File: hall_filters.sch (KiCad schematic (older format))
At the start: 11 parts

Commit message: - updated project to 5.0.0 - added ignore file
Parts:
- C13, C14, C15, C16: symbol C-RESCUE-BLDC_4 -> HSWR-V2-rescue:C-RESCUE-BLDC_4
- R32, R33, R34, R35, R36, R37, R38: symbol R-RESCUE-BLDC_4 -> HSWR-V2-rescue:R-RESCUE-BLDC_4
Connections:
- wire segments 20 -> 31
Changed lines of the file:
@@
-EESchema Schematic File Version 2
-LIBS:HSWR V2-rescue
-LIBS:power
-LIBS:device
-LIBS:transistors
-LIBS:conn
-LIBS:linear
-LIBS:regul
-LIBS:74xx
-LIBS:cmos4000
-LIBS:adc-dac
-LIBS:memory
-LIBS:xilinx
-LIBS:microcontrollers
-LIBS:dsp
-LIBS:microchip
-LIBS:analog_switches
-LIBS:motorola
-LIBS:texas
-LIBS:intel
-LIBS:audio
-LIBS:interface
-LIBS:digital-audio
-LIBS:philips
-LIBS:display
-LIBS:cypress
-LIBS:siliconi
-LIBS:opto
-LIBS:atmel
-LIBS:contrib
-LIBS:valves
+EESchema Schematic File Version 4
 LIBS:HSWR V2-cache
-EELAYER 25 0
+EELAYER 26 0
 EELAYER END
 $Descr A4 11693 8268
@@
 $EndDescr
 $Comp
-L R-RESCUE-BLDC_4 R32
+L HSWR-V2-rescue:R-RESCUE-BLDC_4 R32
 U 1 1 53FBB581
 P 4900 3200
@@
 $EndComp
 $Comp
-L R-RESCUE-BLDC_4 R38
+L HSWR-V2-rescue:R-RESCUE-BLDC_4 R38
 U 1 1 53FBB588
 P 5550 3750
@@
 $EndComp
 $Comp
-L R-RESCUE-BLDC_4 R37
+L HSWR-V2-rescue:R-RESCUE-BLDC_4 R37
 U 1 1 53FBB58F
 P 5550 3650
@@
 $EndComp
 $Comp
-L R-RESCUE-BLDC_4 R36
+L HSWR-V2-rescue:R-RESCUE-BLDC_4 R36
 U 1 1 53FBB596
 P 5550 3550
@@
 $EndComp
 $Comp
-L C-RESCUE-BLDC_4 C14
+L HSWR-V2-rescue:C-RESCUE-BLDC_4 C14
 U 1 1 53FBB59D
 P 5950 4250
@@
 $EndComp
 $Comp
-L C-RESCUE-BLDC_4 C15
+L HSWR-V2-rescue:C-RESCUE-BLDC_4 C15
 U 1 1 53FBB5A4
 P 6200 4250
@@
 $EndComp
 $Comp
-L C-RESCUE-BLDC_4 C16
+L HSWR-V2-rescue:C-RESCUE-BLDC_4 C16
 U 1 1 53FBB5AB
 P 6450 4250
@@
 $EndComp
 $Comp
-L GND-RESCUE-BLDC_4 #PWR034
+L HSWR-V2-rescue:GND-RESCUE-BLDC_4 #PWR034
 U 1 1 53FBB5B2
 P 5950 4450
@@
 $EndComp
 $Comp
-L R-RESCUE-BLDC_4 R33
+L HSWR-V2-rescue:R-RESCUE-BLDC_4 R33
 U 1 1 53FBB5B8
 P 5000 3200
@@
 $EndComp
 $Comp
-L R-RESCUE-BLDC_4 R34
+L HSWR-V2-rescue:R-RESCUE-BLDC_4 R34
 U 1 1 53FBB5BF
 P 5100 3200
@@
 $EndComp
 $Comp
-L R-RESCUE-BLDC_4 R35
+L HSWR-V2-rescue:R-RESCUE-BLDC_4 R35
 U 1 1 53FBB5C6
 P 5200 3200
@@
 $EndComp
 $Comp
-L C-RESCUE-BLDC_4 C13
+L HSWR-V2-rescue:C-RESCUE-BLDC_4 C13
 U 1 1 53FBB5CD
 P 5100 4250
@@
 $EndComp
 $Comp
-L GND-RESCUE-BLDC_4 #PWR035
+L HSWR-V2-rescue:GND-RESCUE-BLDC_4 #PWR035
 U 1 1 53FBB5D4
 P 5100 4450
@@
 	5200 3450 5200 3750
 Wire Wire Line
-	4800 3750 5300 3750
-Wire Wire Line
-	4800 3650 5300 3650
-Wire Wire Line
-	4800 3550 5300 3550
+	4800 3750 5200 3750
+Wire Wire Line
+	4800 3650 5100 3650
+Wire Wire Line
+	4800 3550 5000 3550
 Wire Wire Line
 	6450 3750 6450 4050
 Wire Wire Line
-	5800 3750 6600 3750
+	5800 3750 6450 3750
 Wire Wire Line
 	6200 3650 6200 4050
 Wire Wire Line
-	5800 3650 6600 3650
+	5800 3650 6200 3650
 Wire Wire Line
 	5950 3550 5950 4050
 Wire Wire Line
-	5800 3550 6600 3550
+	5800 3550 5950 3550
 Wire Wire Line
 	5100 3850 5100 4050
 $Comp
-L GND-RESCUE-BLDC_4 #PWR036
+L HSWR-V2-rescue:GND-RESCUE-BLDC_4 #PWR036
 U 1 1 53FBB5F9
 P 6200 4450
@@
 $EndComp
 $Comp
-L GND-RESCUE-BLDC_4 #PWR037
+L HSWR-V2-rescue:GND-RESCUE-BLDC_4 #PWR037
 U 1 1 53FBB5FF
 P 6450 4450
@@
 Connection ~ 4900 3850
 Wire Wire Line
-	4900 2750 4900 2950
-Wire Wire Line
-	4900 2850 5200 2850
+	4900 2750 4900 2850
+Wire Wire Line
+	4900 2850 5000 2850
 Connection ~ 5000 2850
 Connection ~ 5100 2850
 Wire Wire Line
-	4800 3850 6600 3850
+	4800 3850 4900 3850
 Connection ~ 5100 3850
 Text HLabel 4800 3550 0    60   Input ~ 0
@@
 TEMP_OUT
 $Comp
-L +3V3 #PWR038
+L power:+3V3 #PWR038
 U 1 1 5752258C
 P 4900 2750
@@
 $EndComp
 Connection ~ 4900 2850
+Wire Wire Line
+	5950 3550 6600 3550
+Wire Wire Line
+	6200 3650 6600 3650
+Wire Wire Line
+	6450 3750 6600 3750
+Wire Wire Line
+	5000 3550 5300 3550
+Wire Wire Line
+	5100 3650 5300 3650
+Wire Wire Line
+	5200 3750 5300 3750
+Wire Wire Line
+	4900 3850 5100 3850
+Wire Wire Line
+	5000 2850 5100 2850
+Wire Wire Line
+	5100 2850 5200 2850
+Wire Wire Line
+	5100 3850 6600 3850
+Wire Wire Line
+	4900 2850 4900 2950
 $EndSCHEMATC

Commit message: - updated to VESC6 architecture - still some things to do in schematic
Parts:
- removed C13, C14, C15, C16: 4n7, Capacitors_SMD:C_0805, symbol HSWR-V2-rescue:C-RESCUE-BLDC_4
- removed R32, R36, R37, R38: 10k, Resistors_SMD:R_0805, symbol HSWR-V2-rescue:R-RESCUE-BLDC_4
- removed R33, R34, R35: 2k2, Resistors_SMD:R_0805, symbol HSWR-V2-rescue:R-RESCUE-BLDC_4
- added C1, C3, C4, C5: 4n7, Capacitor_SMD:C_0805_2012Metric, symbol Device:C
- added R12, R18, R19, R20: 10k, Resistor_SMD:R_0805_2012Metric, symbol Device:R
- added R13, R14, R15: 2k2, Resistor_SMD:R_0805_2012Metric, symbol Device:R
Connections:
- wire segments 31 -> 30

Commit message: - rescued schematic - added *.sch-bak to ignore - fixed bypass diode polarity - fixed PDEN being low - added 0R resistors instead of USB iso option - added caps to DCDC - added filter to VDDA
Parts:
- C1, C3, C4, C5: symbol Device:C -> HSWR-V2-rescue:C-Device
- R12, R13, R14, R15, R18, R19, R20: symbol Device:R -> HSWR-V2-rescue:R-Device
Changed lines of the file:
@@
 EESchema Schematic File Version 4
-LIBS:HSWR V2-cache
-EELAYER 26 0
+EELAYER 30 0
 EELAYER END
 $Descr A4 11693 8268
@@
 TEMP_OUT
 $Comp
-L power:+3V3 #PWR038
+L HSWR-V2-rescue:+3V3-power #PWR038
 U 1 1 5752258C
 P 4900 2950
@@
 	4900 3050 4900 3150
 $Comp
-L Device:R R?
+L HSWR-V2-rescue:R-Device R?
 U 1 1 5C9EFE99
 P 4900 3300
@@
 $EndComp
 $Comp
-L Device:R R?
+L HSWR-V2-rescue:R-Device R?
 U 1 1 5C9F02C4
 P 5100 3300
@@
 	4800 4050 4900 4050
 $Comp
-L Device:R R?
+L HSWR-V2-rescue:R-Device R?
 U 1 1 5C9F1880
 P 5300 3300
@@
 $EndComp
 $Comp
-L Device:R R?
+L HSWR-V2-rescue:R-Device R?
 U 1 1 5C9F189A
 P 5500 3300
@@
 $EndComp
 $Comp
-L Device:R R?
+L HSWR-V2-rescue:R-Device R?
 U 1 1 5C9F21C4
 P 5750 3550
@@
 $EndComp
 $Comp
-L Device:R R?
+L HSWR-V2-rescue:R-Device R?
 U 1 1 5C9F262F
 P 5750 3750
@@
 $EndComp
 $Comp
-L Device:R R?
+L HSWR-V2-rescue:R-Device R?
 U 1 1 5C9F2B46
 P 5750 3950
@@
 	4900 4050 6700 4050
 $Comp
-L Device:C C3
+L HSWR-V2-rescue:C-Device C3
 U 1 1 5C9F2C75
 P 6050 4300
@@
 $EndComp
 $Comp
-L power:GND #PWR0117
+L HSWR-V2-rescue:GND-power #PWR0117
 U 1 1 5C9F2CD2
 P 6050 4450
@@
 	4900 4050 4900 4150
 $Comp
-L Device:C C1
+L HSWR-V2-rescue:C-Device C1
 U 1 1 5C9F3D39
 P 4900 4300
@@
 $EndComp
 $Comp
-L power:GND #PWR0118
+L HSWR-V2-rescue:GND-power #PWR0118
 U 1 1 5C9F3D40
 P 4900 4450
@@
 $EndComp
 $Comp
-L power:GND #PWR0119
+L HSWR-V2-rescue:GND-power #PWR0119
 U 1 1 5C9F4131
 P 6300 4450
@@
 $EndComp
 $Comp
-L Device:C C4
+L HSWR-V2-rescue:C-Device C4
 U 1 1 5C9F467A
 P 6300 4300
@@
 $EndComp
 $Comp
-L Device:C C5
+L HSWR-V2-rescue:C-Device C5
 U 1 1 5C9F46A6
 P 6550 4300
@@
 $EndComp
 $Comp
-L power:GND #PWR0120
+L HSWR-V2-rescue:GND-power #PWR0120
 U 1 1 5C9F46D2
 P 6550 4450

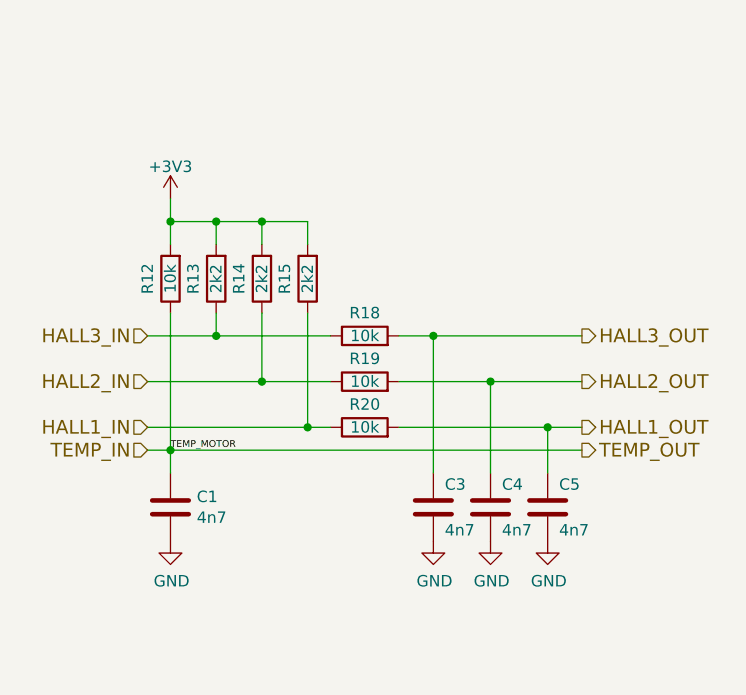
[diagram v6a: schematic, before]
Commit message: - changed CSA for Hall effect sensors - updated power stage layout
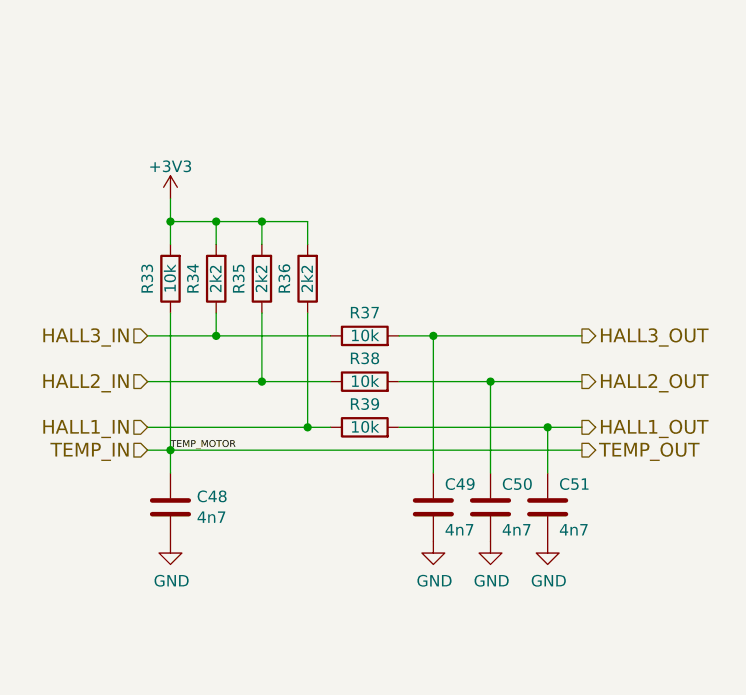
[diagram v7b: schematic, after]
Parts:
- renumbered C1 to C48, C3 to C49, C4 to C50, C5 to C51, R12 to R33, R13 to R34, R14 to R35, R15 to R36, R18 to R37, R19 to R38, R20 to R39
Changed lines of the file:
@@
 TEMP_OUT
 $Comp
-L HSWR-V2-rescue:+3V3-power #PWR038
+L HSWR-V2-rescue:+3V3-power #PWR095
 U 1 1 5752258C
 P 4900 2950
-F 0 "#PWR038" H 4900 2800 50  0001 C CNN
+F 0 "#PWR095" H 4900 2800 50  0001 C CNN
 F 1 "+3V3" H 4900 3090 50  0000 C CNN
 F 2 "" H 4900 2950 60  0000 C CNN
@@
 P 4900 3300
 AR Path="/5895E6A0/5C9EFE99" Ref="R?"  Part="1"
-AR Path="/5899E226/5C9EFE99" Ref="R12"  Part="1"
-F 0 "R12" V 5000 3300 50  0000 C CNN
+AR Path="/5899E226/5C9EFE99" Ref="R33"  Part="1"
+F 0 "R33" V 5000 3300 50  0000 C CNN
 F 1 "10k" V 4900 3300 50  0000 C CNN
 F 2 "Resistor_SMD:R_0805_2012Metric" V 4830 3300 50  0001 C CNN
@@
 P 5100 3300
 AR Path="/5895E6A0/5C9F02C4" Ref="R?"  Part="1"
-AR Path="/5899E226/5C9F02C4" Ref="R13"  Part="1"
-F 0 "R13" V 5200 3300 50  0000 C CNN
+AR Path="/5899E226/5C9F02C4" Ref="R34"  Part="1"
+F 0 "R34" V 5200 3300 50  0000 C CNN
 F 1 "2k2" V 5100 3300 50  0000 C CNN
 F 2 "Resistor_SMD:R_0805_2012Metric" V 5030 3300 50  0001 C CNN
@@
 P 5300 3300
 AR Path="/5895E6A0/5C9F1880" Ref="R?"  Part="1"
-AR Path="/5899E226/5C9F1880" Ref="R14"  Part="1"
-F 0 "R14" V 5400 3300 50  0000 C CNN
+AR Path="/5899E226/5C9F1880" Ref="R35"  Part="1"
+F 0 "R35" V 5400 3300 50  0000 C CNN
 F 1 "2k2" V 5300 3300 50  0000 C CNN
 F 2 "Resistor_SMD:R_0805_2012Metric" V 5230 3300 50  0001 C CNN
@@
 P 5500 3300
 AR Path="/5895E6A0/5C9F189A" Ref="R?"  Part="1"
-AR Path="/5899E226/5C9F189A" Ref="R15"  Part="1"
-F 0 "R15" V 5600 3300 50  0000 C CNN
+AR Path="/5899E226/5C9F189A" Ref="R36"  Part="1"
+F 0 "R36" V 5600 3300 50  0000 C CNN
 F 1 "2k2" V 5500 3300 50  0000 C CNN
 F 2 "Resistor_SMD:R_0805_2012Metric" V 5430 3300 50  0001 C CNN
@@
 P 5750 3550
 AR Path="/5895E6A0/5C9F21C4" Ref="R?"  Part="1"
-AR Path="/5899E226/5C9F21C4" Ref="R18"  Part="1"
-F 0 "R18" V 5850 3550 50  0000 C CNN
+AR Path="/5899E226/5C9F21C4" Ref="R37"  Part="1"
+F 0 "R37" V 5850 3550 50  0000 C CNN
 F 1 "10k" V 5750 3550 50  0000 C CNN
 F 2 "Resistor_SMD:R_0805_2012Metric" V 5680 3550 50  0001 C CNN
@@
 P 5750 3750
 AR Path="/5895E6A0/5C9F262F" Ref="R?"  Part="1"
-AR Path="/5899E226/5C9F262F" Ref="R19"  Part="1"
-F 0 "R19" V 5850 3750 50  0000 C CNN
+AR Path="/5899E226/5C9F262F" Ref="R38"  Part="1"
+F 0 "R38" V 5850 3750 50  0000 C CNN
 F 1 "10k" V 5750 3750 50  0000 C CNN
 F 2 "Resistor_SMD:R_0805_2012Metric" V 5680 3750 50  0001 C CNN
@@
 P 5750 3950
 AR Path="/5895E6A0/5C9F2B46" Ref="R?"  Part="1"
-AR Path="/5899E226/5C9F2B46" Ref="R20"  Part="1"
-F 0 "R20" V 5850 3950 50  0000 C CNN
+AR Path="/5899E226/5C9F2B46" Ref="R39"  Part="1"
+F 0 "R39" V 5850 3950 50  0000 C CNN
 F 1 "10k" V 5750 3950 50  0000 C CNN
 F 2 "Resistor_SMD:R_0805_2012Metric" V 5680 3950 50  0001 C CNN
@@
 	4900 4050 6700 4050
 $Comp
-L HSWR-V2-rescue:C-Device C3
+L HSWR-V2-rescue:C-Device C49
 U 1 1 5C9F2C75
 P 6050 4300
-F 0 "C3" H 6100 4400 50  0000 L CNN
+F 0 "C49" H 6100 4400 50  0000 L CNN
 F 1 "4n7" H 6100 4200 50  0000 L CNN
 F 2 "Capacitor_SMD:C_0805_2012Metric" H 6088 4150 50  0001 C CNN
@@
 $EndComp
 $Comp
-L HSWR-V2-rescue:GND-power #PWR0117
+L HSWR-V2-rescue:GND-power #PWR097
 U 1 1 5C9F2CD2
 P 6050 4450
-F 0 "#PWR0117" H 6050 4200 50  0001 C CNN
+F 0 "#PWR097" H 6050 4200 50  0001 C CNN
 F 1 "GND" H 6055 4277 50  0000 C CNN
 F 2 "" H 6050 4450 50  0001 C CNN
@@
 	4900 4050 4900 4150
 $Comp
-L HSWR-V2-rescue:C-Device C1
+L HSWR-V2-rescue:C-Device C48
 U 1 1 5C9F3D39
 P 4900 4300
-F 0 "C1" H 5015 4346 50  0000 L CNN
+F 0 "C48" H 5015 4346 50  0000 L CNN
 F 1 "4n7" H 5015 4255 50  0000 L CNN
 F 2 "Capacitor_SMD:C_0805_2012Metric" H 4938 4150 50  0001 C CNN
@@
 $EndComp
 $Comp
-L HSWR-V2-rescue:GND-power #PWR0118
+L HSWR-V2-rescue:GND-power #PWR096
 U 1 1 5C9F3D40
 P 4900 4450
-F 0 "#PWR0118" H 4900 4200 50  0001 C CNN
+F 0 "#PWR096" H 4900 4200 50  0001 C CNN
 F 1 "GND" H 4905 4277 50  0000 C CNN
 F 2 "" H 4900 4450 50  0001 C CNN
@@
 $EndComp
 $Comp
-L HSWR-V2-rescue:GND-power #PWR0119
+L HSWR-V2-rescue:GND-power #PWR098
 U 1 1 5C9F4131
 P 6300 4450
-F 0 "#PWR0119" H 6300 4200 50  0001 C CNN
+F 0 "#PWR098" H 6300 4200 50  0001 C CNN
 F 1 "GND" H 6305 4277 50  0000 C CNN
 F 2 "" H 6300 4450 50  0001 C CNN
@@
 $EndComp
 $Comp
-L HSWR-V2-rescue:C-Device C4
+L HSWR-V2-rescue:C-Device C50
 U 1 1 5C9F467A
 P 6300 4300
-F 0 "C4" H 6350 4400 50  0000 L CNN
+F 0 "C50" H 6350 4400 50  0000 L CNN
 F 1 "4n7" H 6350 4200 50  0000 L CNN
 F 2 "Capacitor_SMD:C_0805_2012Metric" H 6338 4150 50  0001 C CNN
@@
 $EndComp
 $Comp
-L HSWR-V2-rescue:C-Device C5
+L HSWR-V2-rescue:C-Device C51
 U 1 1 5C9F46A6
 P 6550 4300
-F 0 "C5" H 6600 4400 50  0000 L CNN
+F 0 "C51" H 6600 4400 50  0000 L CNN
 F 1 "4n7" H 6600 4200 50  0000 L CNN
 F 2 "Capacitor_SMD:C_0805_2012Metric" H 6588 4150 50  0001 C CNN
@@
 $EndComp
 $Comp
-L HSWR-V2-rescue:GND-power #PWR0120
+L HSWR-V2-rescue:GND-power #PWR099
 U 1 1 5C9F46D2
 P 6550 4450
-F 0 "#PWR0120" H 6550 4200 50  0001 C CNN
+F 0 "#PWR099" H 6550 4200 50  0001 C CNN
 F 1 "GND" H 6555 4277 50  0000 C CNN
 F 2 "" H 6550 4450 50  0001 C CNN

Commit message: - removed rescue lib and symbols - added HSWR.lib
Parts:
- C48, C49, C50, C51: symbol HSWR-V2-rescue:C-Device -> Device:C
- R33, R34, R35, R36, R37, R38, R39: symbol HSWR-V2-rescue:R-Device -> Device:R
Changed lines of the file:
@@
 $Descr A4 11693 8268
 encoding utf-8
-Sheet 6 8
+Sheet 5 8
 Title "HSWR HAL Filters"
 Date "2017-02-05"
@@
 TEMP_OUT
 $Comp
-L HSWR-V2-rescue:+3V3-power #PWR095
+L power:+3V3 #PWR095
 U 1 1 5752258C
 P 4900 2950
@@
 	4900 3050 4900 3150
 $Comp
-L HSWR-V2-rescue:R-Device R?
+L Device:R R?
 U 1 1 5C9EFE99
 P 4900 3300
@@
 $EndComp
 $Comp
-L HSWR-V2-rescue:R-Device R?
+L Device:R R?
 U 1 1 5C9F02C4
 P 5100 3300
@@
 	4800 4050 4900 4050
 $Comp
-L HSWR-V2-rescue:R-Device R?
+L Device:R R?
 U 1 1 5C9F1880
 P 5300 3300
@@
 $EndComp
 $Comp
-L HSWR-V2-rescue:R-Device R?
+L Device:R R?
 U 1 1 5C9F189A
 P 5500 3300
@@
 $EndComp
 $Comp
-L HSWR-V2-rescue:R-Device R?
+L Device:R R?
 U 1 1 5C9F21C4
 P 5750 3550
@@
 $EndComp
 $Comp
-L HSWR-V2-rescue:R-Device R?
+L Device:R R?
 U 1 1 5C9F262F
 P 5750 3750
@@
 $EndComp
 $Comp
-L HSWR-V2-rescue:R-Device R?
+L Device:R R?
 U 1 1 5C9F2B46
 P 5750 3950
@@
 	4900 4050 6700 4050
 $Comp
-L HSWR-V2-rescue:C-Device C49
+L Device:C C49
 U 1 1 5C9F2C75
 P 6050 4300
@@
 $EndComp
 $Comp
-L HSWR-V2-rescue:GND-power #PWR097
+L power:GND #PWR097
 U 1 1 5C9F2CD2
 P 6050 4450
@@
 	4900 4050 4900 4150
 $Comp
-L HSWR-V2-rescue:C-Device C48
+L Device:C C48
 U 1 1 5C9F3D39
 P 4900 4300
@@
 $EndComp
 $Comp
-L HSWR-V2-rescue:GND-power #PWR096
+L power:GND #PWR096
 U 1 1 5C9F3D40
 P 4900 4450
@@
 $EndComp
 $Comp
-L HSWR-V2-rescue:GND-power #PWR098
+L power:GND #PWR098
 U 1 1 5C9F4131
 P 6300 4450
@@
 $EndComp
 $Comp
-L HSWR-V2-rescue:C-Device C50
+L Device:C C50
 U 1 1 5C9F467A
 P 6300 4300
@@
 $EndComp
 $Comp
-L HSWR-V2-rescue:C-Device C51
+L Device:C C51
 U 1 1 5C9F46A6
 P 6550 4300
@@
 $EndComp
 $Comp
-L HSWR-V2-rescue:GND-power #PWR099
+L power:GND #PWR099
 U 1 1 5C9F46D2
 P 6550 4450
